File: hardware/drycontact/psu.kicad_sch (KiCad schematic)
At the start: 11 parts, among them J4 DC IN 12-24V, U5 TPS54202DDCR, U6 LM1117IMP-3.3

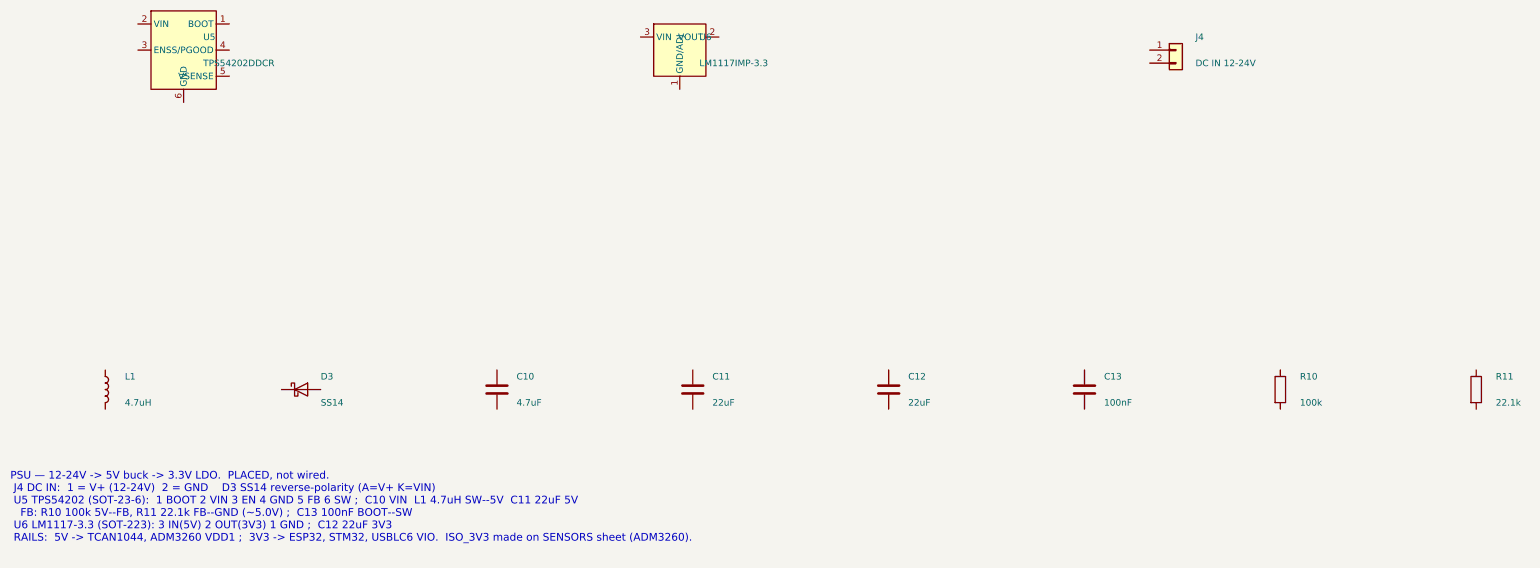
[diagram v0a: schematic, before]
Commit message: hardware: place parts for DryContact, PlugControl, SensorBuddy
Generate each board's schematic from a scripts/<board>.schgen.py manifest —
every part resolves to a real KiCad symbol + matching footprint + 3D model + LCSC.
Parts are PLACED, not wired (wire in eeschema; each sheet carries a pinout note).
make check-<board> = structure sound for all three:
- DryContact  (NEW): 49 components — STM32G0B1 + TCAN1044 + ULN2003 + 4x Omron
  G6K-2F-Y Form-C dry contacts; 29-bit CAN, UID auto-address. + BOM + handsolder.
- PlugControl (NEW KiCad project): 88 components — mcu/safety/actuation. A few
  generic stand-in symbols (TLV3202/74HC08/REF3330/TPS3823/SSR) pending swap;
  footprints/LCSC are correct.
- SensorBuddy (regenerated from placeholders): 81 components — ESP32-S3 + STM32G0B1
  + isolated ADM3260/ADS1115/OPA2376 probe front-end + NTC/1-Wire/floats.
Reuses the existing custom symbols in lib/symbols/sensorbuddy.kicad_sym.

Co-Authored-By: Claude Opus 4.8 (1M context) <noreply@anthropic.com>
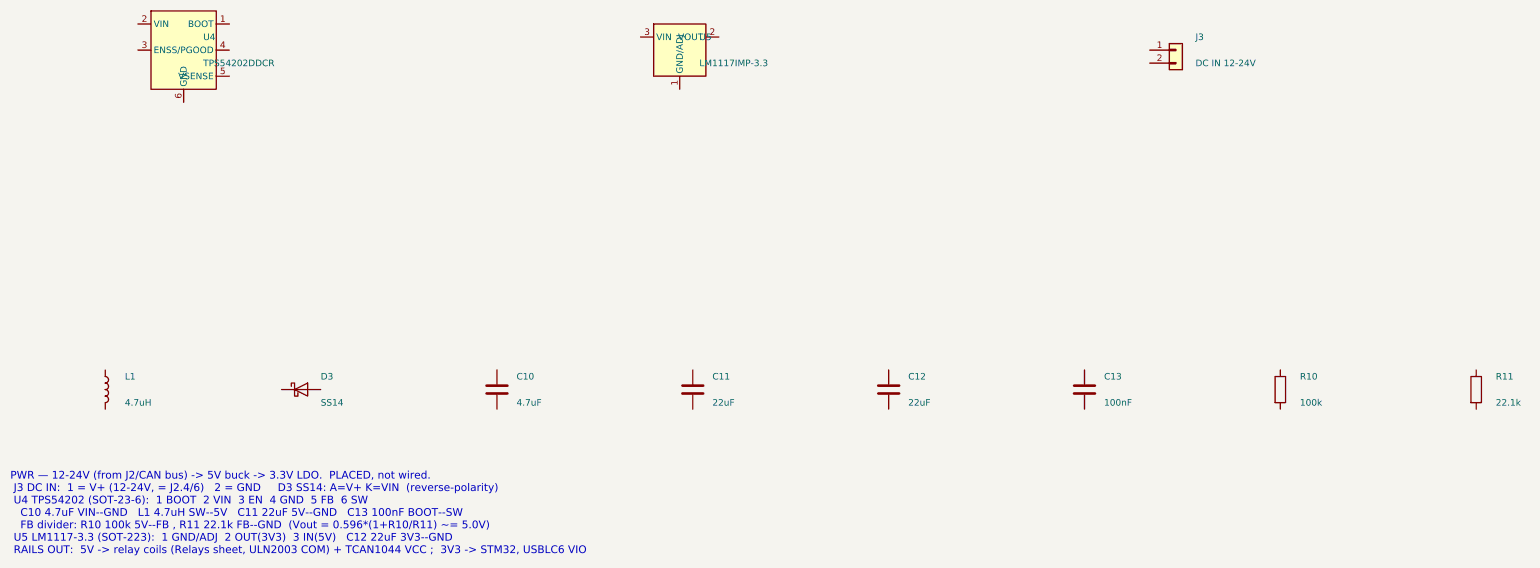
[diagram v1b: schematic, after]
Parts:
- removed J4: DC IN 12-24V, TerminalBlock_Phoenix:TerminalBlock_Phoenix_MPT-0,5-2-2.54_1x02_P2.54mm_Horizontal, symbol Connector_Generic:Conn_01x02
- removed U5: TPS54202DDCR, Package_TO_SOT_SMD:SOT-23-6, symbol sensorbuddy:TPS54202DDCR
- removed U6: LM1117IMP-3.3, Package_TO_SOT_SMD:SOT-223-3_TabPin2, symbol sensorbuddy:LM1117IMP-3.3
- added J3: DC IN 12-24V, TerminalBlock_Phoenix:TerminalBlock_Phoenix_MPT-0,5-2-2.54_1x02_P2.54mm_Horizontal, symbol Connector_Generic:Conn_01x02
- added U4: TPS54202DDCR, Package_TO_SOT_SMD:SOT-23-6, symbol sensorbuddy:TPS54202DDCR
- added U5: LM1117IMP-3.3, Package_TO_SOT_SMD:SOT-223-3_TabPin2, symbol sensorbuddy:LM1117IMP-3.3
- C10: LCSC C19666 -> C1611
- C13: footprint Capacitor_SMD:C_0603_1608Metric -> Capacitor_SMD:C_0402_1005Metric; LCSC C14663 -> C1525
- R10: footprint Resistor_SMD:R_0603_1608Metric -> Resistor_SMD:R_0402_1005Metric; LCSC C25803 -> C25741
- R11: footprint Resistor_SMD:R_0603_1608Metric -> Resistor_SMD:R_0402_1005Metric
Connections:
- new net: U5.2 (VOUT), U5.4 (VOUT)
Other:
- note added: "PWR — 12-24V (from J2/CAN bus) -> 5V buck -> 3.3V LDO. PLACED, not wired. J3 DC IN: 1 = V+ (12-24V, = J2.4/6) 2 = GND D3 SS14: A=V+ K=VIN (reverse-polarity) U4 TPS54202 (SOT-23-6): 1 BOOT 2 VIN 3 EN 4 GND 5 FB 6 SW C10 4.7uF VIN--GND L1 4.7uH SW--5V C11 22uF 5V--GND C13 100nF BOOT--SW FB divider: R10 100k 5V--FB , R11 22.1k FB--GND (Vout = 0.596*(1+R10/R11) ~= 5.0V) U5 LM1117-3.3 (SOT-223): 1 GND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"
- note removed: "PSU — 12-24V -> 5V buck -> 3.3V LDO. PLACED, not wired. J4 DC IN: 1 = V+ (12-24V) 2 = GND D3 SS14 reverse-polarity (A=V+ K=VIN) U5 TPS54202 (SOT-23-6): 1 BOOT 2 VIN 3 EN 4 GND 5 FB 6 SW ; C10 VIN L1 4.7uH SW--5V C11 22uF 5V FB: R10 100k 5V--FB, R11 22.1k FB--GND (~5.0V) ; C13 100nF BOOT--SW U6 LM1117-3.3 (SOT-223): 3 IN(5V) 2 OUT(3V3) 1 GND ; C12 22uF 3V3 RAILS: 5V -> TCAN1044, ADM3260 VDD1 ; 3V3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"
- title: ReefVolt SensorBuddy — Main — Power: 12-24V -> TPS54202 5V -> LM1117 3.3V (+ barrel/Phoenix in) -> ReefVolt DryContact — 4ch Form-C carrier — Power: 12-24V (CAN bus) -> TPS54202 5V -> LM1117 3.3V
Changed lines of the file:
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@@
 	(paper "A3")
 	(title_block
-		(title "ReefVolt SensorBuddy — Main — Power: 12-24V -> TPS54202 5V -> LM1117 3.3V (+ barrel/Phoenix in)")
+		(title "ReefVolt DryContact — 4ch Form-C carrier — Power: 12-24V (CAN bus) -> TPS54202 5V -> LM1117 3.3V")
 		(date "2026-07-04")
 		(rev "0.1")
@@
 		(on_board yes)
 		(dnp no)
-		(property "Reference" "U5"
+		(property "Reference" "U4"
 			(at 49.5300 53.3400 0)
 			(effects (font (size 1.27 1.27)) (justify left))
@@
 		(pin "6")
 		(instances
-			(project "sensorbuddy"
-				(path "/a1b2c3d4-e5f6-7890-abcd-ef0123456789/f52a4ed5-c1a0-4069-8c26-21979fcdfc09"
-					(reference "U5")
+			(project "drycontact"
+				(path "/d0000000-0000-4dc0-8000-000000000001/345e2863-c1ad-4a65-acd6-35ac944868d2"
+					(reference "U4")
 					(unit 1)
 				)
@@
 		(on_board yes)
 		(dnp no)
-		(property "Reference" "U6"
+		(property "Reference" "U5"
 			(at 146.0500 53.3400 0)
 			(effects (font (size 1.27 1.27)) (justify left))
@@
 		(pin "4")
 		(instances
-			(project "sensorbuddy"
-				(path "/a1b2c3d4-e5f6-7890-abcd-ef0123456789/f52a4ed5-c1a0-4069-8c26-21979fcdfc09"
-					(reference "U6")
+			(project "drycontact"
+				(path "/d0000000-0000-4dc0-8000-000000000001/345e2863-c1ad-4a65-acd6-35ac944868d2"
+					(reference "U5")
 					(unit 1)
 				)
@@
 		(on_board yes)
 		(dnp no)
-		(property "Reference" "J4"
+		(property "Reference" "J3"
 			(at 242.5700 53.3400 0)
 			(effects (font (size 1.27 1.27)) (justify left))
@@
 		(pin "2")
 		(instances
-			(project "sensorbuddy"
-				(path "/a1b2c3d4-e5f6-7890-abcd-ef0123456789/f52a4ed5-c1a0-4069-8c26-21979fcdfc09"
-					(reference "J4")
+			(project "drycontact"
+				(path "/d0000000-0000-4dc0-8000-000000000001/345e2863-c1ad-4a65-acd6-35ac944868d2"
+					(reference "J3")
 					(unit 1)
 				)
@@
 		(pin "2")
 		(instances
-			(project "sensorbuddy"
-				(path "/a1b2c3d4-e5f6-7890-abcd-ef0123456789/f52a4ed5-c1a0-4069-8c26-21979fcdfc09"
+			(project "drycontact"
+				(path "/d0000000-0000-4dc0-8000-000000000001/345e2863-c1ad-4a65-acd6-35ac944868d2"
 					(reference "L1")
 					(unit 1)
@@
 		(pin "2")
 		(instances
-			(project "sensorbuddy"
-				(path "/a1b2c3d4-e5f6-7890-abcd-ef0123456789/f52a4ed5-c1a0-4069-8c26-21979fcdfc09"
+			(project "drycontact"
+				(path "/d0000000-0000-4dc0-8000-000000000001/345e2863-c1ad-4a65-acd6-35ac944868d2"
 					(reference "D3")
 					(unit 1)
@@
 			(effects (font (size 1.27 1.27))) (hide yes)
 		)
-		(property "LCSC" "C19666"
+		(property "LCSC" "C1611"
 			(at 106.6800 121.9200 0)
 			(effects (font (size 1.27 1.27))) (hide yes)
@@
 		(pin "2")
 		(instances
-			(project "sensorbuddy"
-				(path "/a1b2c3d4-e5f6-7890-abcd-ef0123456789/f52a4ed5-c1a0-4069-8c26-21979fcdfc09"
+			(project "drycontact"
+				(path "/d0000000-0000-4dc0-8000-000000000001/345e2863-c1ad-4a65-acd6-35ac944868d2"
 					(reference "C10")
 					(unit 1)
@@
 		(pin "2")
 		(instances
-			(project "sensorbuddy"
-				(path "/a1b2c3d4-e5f6-7890-abcd-ef0123456789/f52a4ed5-c1a0-4069-8c26-21979fcdfc09"
+			(project "drycontact"
+				(path "/d0000000-0000-4dc0-8000-000000000001/345e2863-c1ad-4a65-acd6-35ac944868d2"
 					(reference "C11")
 					(unit 1)
@@
 		(pin "2")
 		(instances
-			(project "sensorbuddy"
-				(path "/a1b2c3d4-e5f6-7890-abcd-ef0123456789/f52a4ed5-c1a0-4069-8c26-21979fcdfc09"
+			(project "drycontact"
+				(path "/d0000000-0000-4dc0-8000-000000000001/345e2863-c1ad-4a65-acd6-35ac944868d2"
 					(reference "C12")
 					(unit 1)
@@
 			(effects (font (size 1.27 1.27)) (justify left))
 		)
-		(property "Footprint" "Capacitor_SMD:C_0603_1608Metric"
+		(property "Footprint" "Capacitor_SMD:C_0402_1005Metric"
 			(at 220.9800 121.9200 0)
 			(effects (font (size 1.27 1.27))) (hide yes)
@@
 			(effects (font (size 1.27 1.27))) (hide yes)
 		)
-		(property "LCSC" "C14663"
+		(property "LCSC" "C1525"
 			(at 220.9800 121.9200 0)
 			(effects (font (size 1.27 1.27))) (hide yes)
@@
 		(pin "2")
 		(instances
-			(project "sensorbuddy"
-				(path "/a1b2c3d4-e5f6-7890-abcd-ef0123456789/f52a4ed5-c1a0-4069-8c26-21979fcdfc09"
+			(project "drycontact"
+				(path "/d0000000-0000-4dc0-8000-000000000001/345e2863-c1ad-4a65-acd6-35ac944868d2"
 					(reference "C13")
 					(unit 1)
@@
 			(effects (font (size 1.27 1.27)) (justify left))
 		)
-		(property "Footprint" "Resistor_SMD:R_0603_1608Metric"
+		(property "Footprint" "Resistor_SMD:R_0402_1005Metric"
 			(at 259.0800 121.9200 0)
 			(effects (font (size 1.27 1.27))) (hide yes)
@@
 			(effects (font (size 1.27 1.27))) (hide yes)
 		)
-		(property "LCSC" "C25803"
+		(property "LCSC" "C25741"
 			(at 259.0800 121.9200 0)
 			(effects (font (size 1.27 1.27))) (hide yes)
@@
 		(pin "2")
 		(instances
-			(project "sensorbuddy"
-				(path "/a1b2c3d4-e5f6-7890-abcd-ef0123456789/f52a4ed5-c1a0-4069-8c26-21979fcdfc09"
+			(project "drycontact"
+				(path "/d0000000-0000-4dc0-8000-000000000001/345e2863-c1ad-4a65-acd6-35ac944868d2"
 					(reference "R10")
 					(unit 1)
@@
 			(effects (font (size 1.27 1.27)) (justify left))
 		)
-		(property "Footprint" "Resistor_SMD:R_0603_1608Metric"
+		(property "Footprint" "Resistor_SMD:R_0402_1005Metric"
 			(at 297.1800 121.9200 0)
 			(effects (font (size 1.27 1.27))) (hide yes)
@@
 		(pin "2")
 		(instances
-			(project "sensorbuddy"
-				(path "/a1b2c3d4-e5f6-7890-abcd-ef0123456789/f52a4ed5-c1a0-4069-8c26-21979fcdfc09"
+			(project "drycontact"
+				(path "/d0000000-0000-4dc0-8000-000000000001/345e2863-c1ad-4a65-acd6-35ac944868d2"
 					(reference "R11")
 					(unit 1)
@@
 		)
 	)
-	(text "PSU — 12-24V -> 5V buck -> 3.3V LDO.  PLACED, not wired.\n J4 DC IN:  1 = V+ (12-24V)  2 = GND    D3 SS14 reverse-polarity (A=V+ K=VIN)\n U5 TPS54202 (SOT-23-6):  1 BOOT 2 VIN 3 EN 4 GND 5 FB 6 SW ;  C10 VIN  L1 4.7uH SW--5V  C11 22uF 5V\n   FB: R10 100k 5V--FB, R11 22.1k FB--GND (~5.0V) ;  C13 100nF BOOT--SW\n U6 LM1117-3.3 (SOT-223): 3 IN(5V) 2 OUT(3V3) 1 GND ;  C12 22uF 3V3\n RAILS:  5V -> TCAN1044, ADM3260 VDD1 ;  3V3 -> ESP32, STM32, USBLC6 VIO.  ISO_3V3 made on SENSORS sheet (ADM3260)."
+	(text "PWR — 12-24V (from J2/CAN bus) -> 5V buck -> 3.3V LDO.  PLACED, not wired.\n J3 DC IN:  1 = V+ (12-24V, = J2.4/6)   2 = GND     D3 SS14: A=V+ K=VIN  (reverse-polarity)\n U4 TPS54202 (SOT-23-6):  1 BOOT  2 VIN  3 EN  4 GND  5 FB  6 SW\n   C10 4.7uF VIN--GND   L1 4.7uH SW--5V   C11 22uF 5V--GND   C13 100nF BOOT--SW\n   FB divider: R10 100k 5V--FB , R11 22.1k FB--GND  (Vout = 0.596*(1+R10/R11) ~= 5.0V)\n U5 LM1117-3.3 (SOT-223):  1 GND/ADJ  2 OUT(3V3)  3 IN(5V)   C12 22uF 3V3--GND\n RAILS OUT:  5V -> relay coils (Relays sheet, ULN2003 COM) + TCAN1044 VCC ;  3V3 -> STM32, USBLC6 VIO"
 		(exclude_from_sim no)
 		(at 12.00 137.92 0)
@@
 	(sheet_instances
 		(path "/"
-			(page "2")
-		)
-	)
+			(page "3")
+		)
+	)
